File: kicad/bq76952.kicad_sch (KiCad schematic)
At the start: 61 parts, among them Q1 FCX495TA, U4 BQ76952

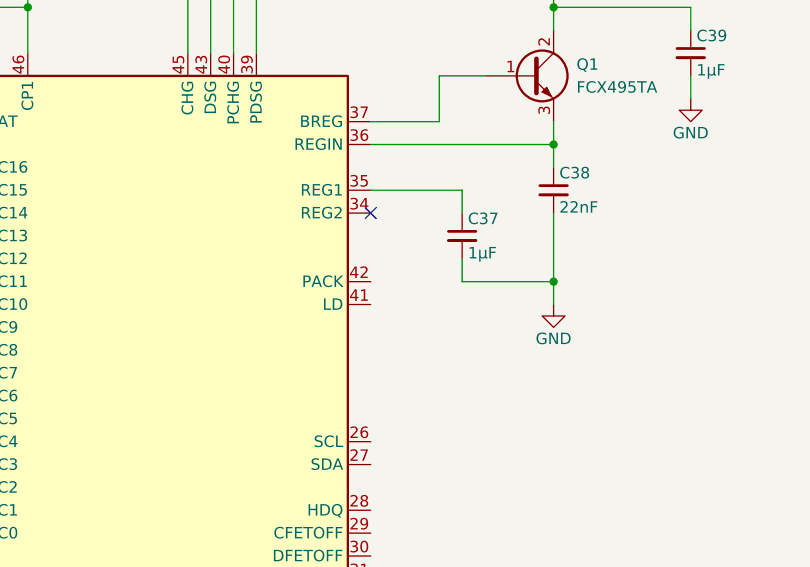
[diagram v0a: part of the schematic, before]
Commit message: Update KiCad files based on spec updates
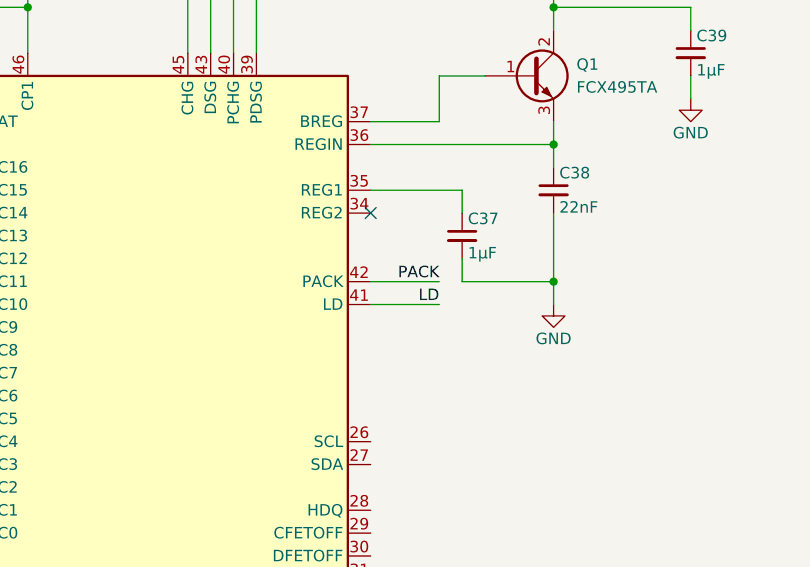
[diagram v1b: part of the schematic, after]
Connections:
- net LD: now reaches U4.41 (LD)
- net PACK: now reaches U4.42 (PACK)
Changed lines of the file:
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@@
     (stroke (width 0) (type solid) (color 0 0 0 0))
+  )
+  (wire (pts (xy 149.86 68.58) (xy 157.48 68.58))
+    (stroke (width 0) (type default) (color 0 0 0 0))
   )
   (wire (pts (xy 256.54 66.04) (xy 256.54 68.58))
@@
   (wire (pts (xy 38.1 43.18) (xy 40.64 43.18))
     (stroke (width 0) (type solid) (color 0 0 0 0))
+  )
+  (wire (pts (xy 149.86 71.12) (xy 157.48 71.12))
+    (stroke (width 0) (type default) (color 0 0 0 0))
   )
   (wire (pts (xy 38.1 165.1) (xy 40.64 165.1))
@@
     (effects (font (size 2.54 2.54)) (justify left bottom))
   )
+  (label "PACK" (at 157.48 68.58 180)
+    (effects (font (size 1.27 1.27)) (justify right bottom))
+  )
   (label "VC13" (at 96.52 63.5 0)
     (effects (font (size 1.27 1.27)) (justify left bottom))
@@
     (effects (font (size 1.27 1.27)) (justify left bottom))
   )
+  (label "LD" (at 157.48 71.12 180)
+    (effects (font (size 1.27 1.27)) (justify right bottom))
+  )
   (hierarchical_label "CELL5+" (shape input) (at 38.1 134.62 180)

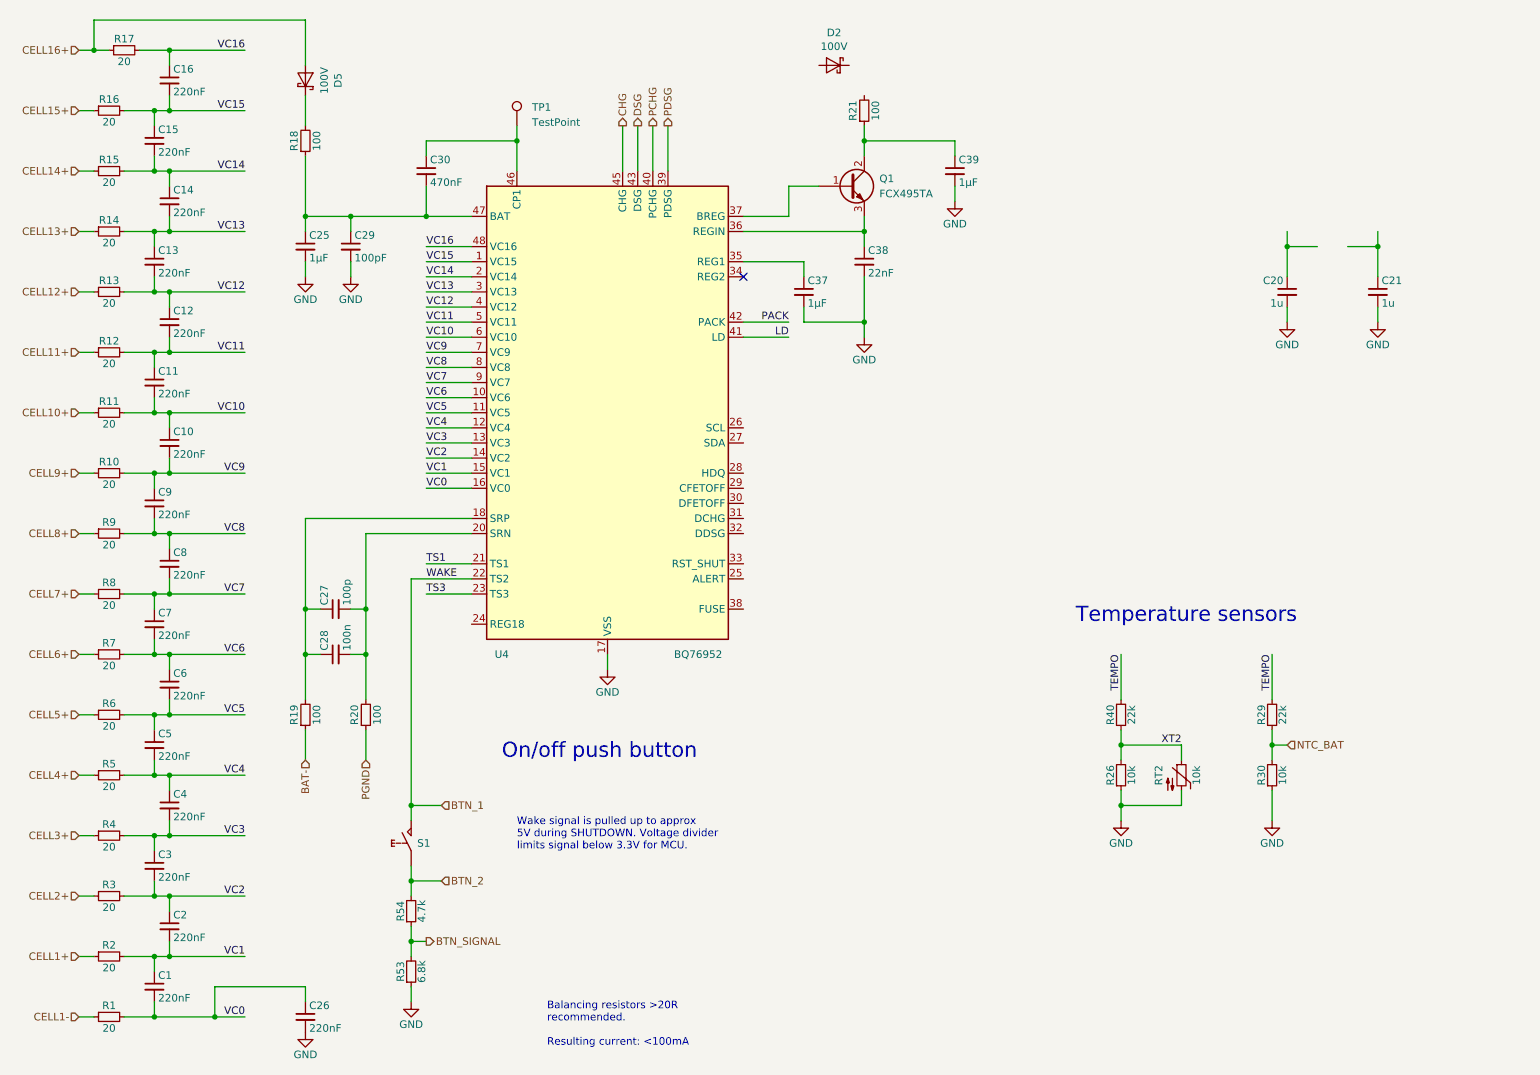
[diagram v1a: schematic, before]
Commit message: WIP: Schematic almost finished
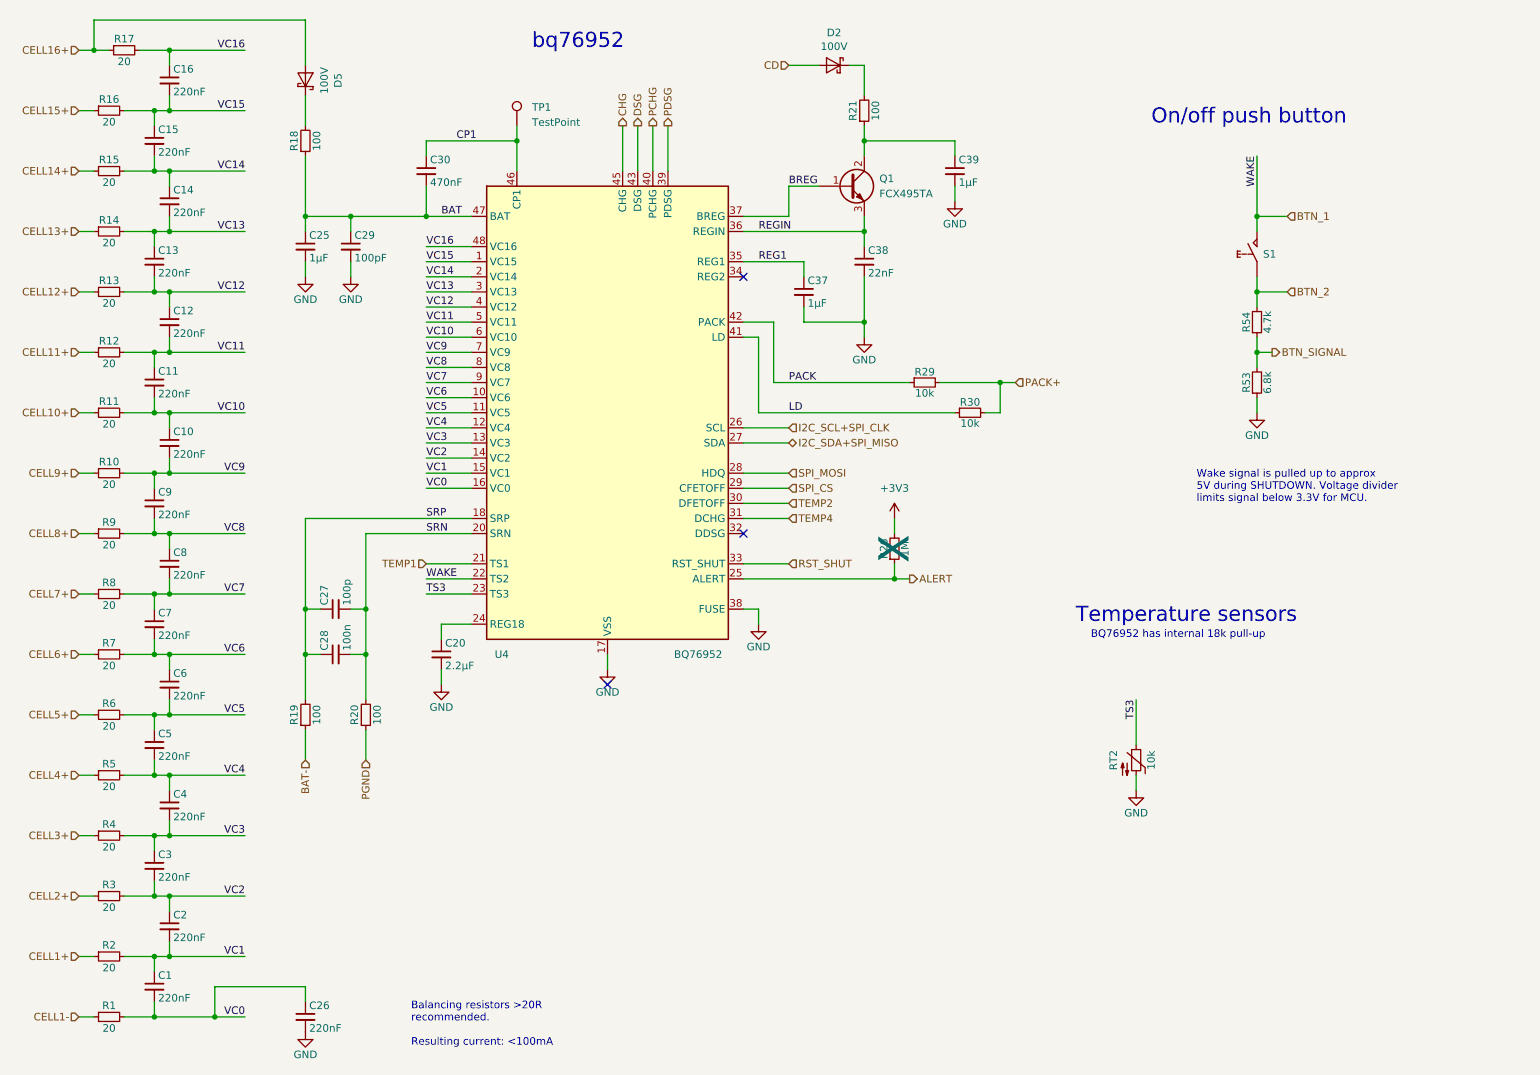
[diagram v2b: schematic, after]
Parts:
- removed C21: 1u, LibreSolar:C_0603_1608, symbol LibreSolar:C
- removed R40: 22k, LibreSolar:R_0603_1608, symbol LibreSolar:R
- C20: value 1u -> 2.2µF; Manufacturer Murata -> any; PartNumber GRT188R61H105KE13D -> (none); Remarks 50V, X5R -> X7R, 6.3V
- R26: value 10k -> 1M; DNM (none) -> X; Manufacturer Yageo -> any; PartNumber RC0603FR-0710KL -> (none)
- R29: value 22k -> 10k; PartNumber RC0603FR-0722KL -> RC0603FR-0710KL
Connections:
- net TEMPO is gone; now on net PACK+: R29.2
- net GND: now also U4.38 (FUSE); no longer R26.1, R30.1
- net LD: now also R30.1
- net PACK: now also R29.1
- net TS3: now also RT2.1
- net SRP: now reaches C27.1, C28.1, R19.2, U4.18 (SRP)
- net SRN: now reaches C27.2, C28.2, R20.2, U4.20 (SRN)
- net at C20.1: now also U4.24 (REG18)
- net BREG: now reaches Q1.1 (B), U4.37 (BREG)
- net REGIN: now reaches C38.1, Q1.3 (E), U4.36 (REGIN)
- net CP1: now reaches C30.1, TP1.1, U4.46 (CP1)
- net BAT: now reaches C25.1, C29.1, C30.2, R18.1, U4.47 (BAT)
- net at R21.2: now also D2.1 (K)
- net CD: now reaches D2.2 (A)
- net ALERT: now reaches U4.25 (ALERT)
- net ALERT: now also R26.1
- net I2C_SCL+SPI_CLK: now reaches U4.26 (SCL)
- net I2C_SDA+SPI_MISO: now reaches U4.27 (SDA)
- net SPI_MOSI: now reaches U4.28 (HDQ)
- net SPI_CS: now reaches U4.29 (CFETOFF)
- net TEMP2: now reaches U4.30 (DFETOFF)
- net TEMP4: now reaches U4.31 (DCHG)
- net RST_SHUT: now reaches U4.33 (RST_SHUT)
- net REG1: now reaches C37.1, U4.35 (REG1)
- net NTC_BAT renamed PACK+
- net PACK+: no longer R29.1
- net TS1 renamed TEMP1
- net XT2 renamed +3V3
- net +3V3: no longer RT2.1
- no-connect marks 1 -> 3
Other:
- note added: "BQ76952 has internal 18k pull-up"
- note added: "bq76952"
- title: BMS 8S50 IC -> BMS 16S Control Board
- moved on the sheet: R53, R54, RT2, S1

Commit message: v0.1 design ready for review
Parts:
- added C44: 1µF, LibreSolar:C_0603_1608, symbol LibreSolar:C
- added C45: 100pF, LibreSolar:C_0603_1608, symbol LibreSolar:C
- added D6: D_Schottky, Diode_SMD:D_SOD-123F, symbol Device:D_Schottky
- added TP15: WAKE, TestPoint:TestPoint_Pad_D1.5mm, symbol Connector:TestPoint
- C27: value 100p -> 100pF; Manufacturer (none) -> any; Remarks (none) -> 100V, C0G/NP0
- C28: value 100n -> 100nF; Manufacturer (none) -> any
- C30: value 470nF -> 680nF
- R18, R21: footprint LibreSolar:R_0603_1608 -> LibreSolar:R_1206_3216
- R29, R30: Manufacturer Yageo -> any; PartNumber RC0603FR-0710KL -> (none)
- R53: Manufacturer Yageo -> any; PartNumber RC0603FR-071ML -> (none)
- R54: Manufacturer Yageo -> any; PartNumber RC0603FR-071KL -> (none)
- TP1: footprint TestPoint:TestPoint_Pad_D2.0mm -> TestPoint:TestPoint_Pad_D1.5mm
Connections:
- net BTN_1: now also TP15.1
- net GND: now also C44.2, C45.2
- net TS3: now also C45.1
- net BREG_IN: now reaches C39.1, Q1.2 (C), R21.1
- net REG2: now reaches U4.34 (REG2)
- net REG2: now also C44.1, D6.2 (A)
- net PCHG: no longer names the net of U4.40 (PCHG)
- net PGND renamed PACK-
- new net +5V: D6.1 (K)
- no-connect marks 3 -> 2
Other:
- note added: "Maximum C_iss of IPT015N10N5 = 16nF CP capacity estimation: 4 x 16nF x 10 = 640nF"
- note added: "Preliminary power supply for MCU after wake-up (see TI reference design) (alternative: REG1 enabling the SMPS)"
- note added: "WAKE"
- moved on the sheet: C27, C38, C39, D2, Q1, R21

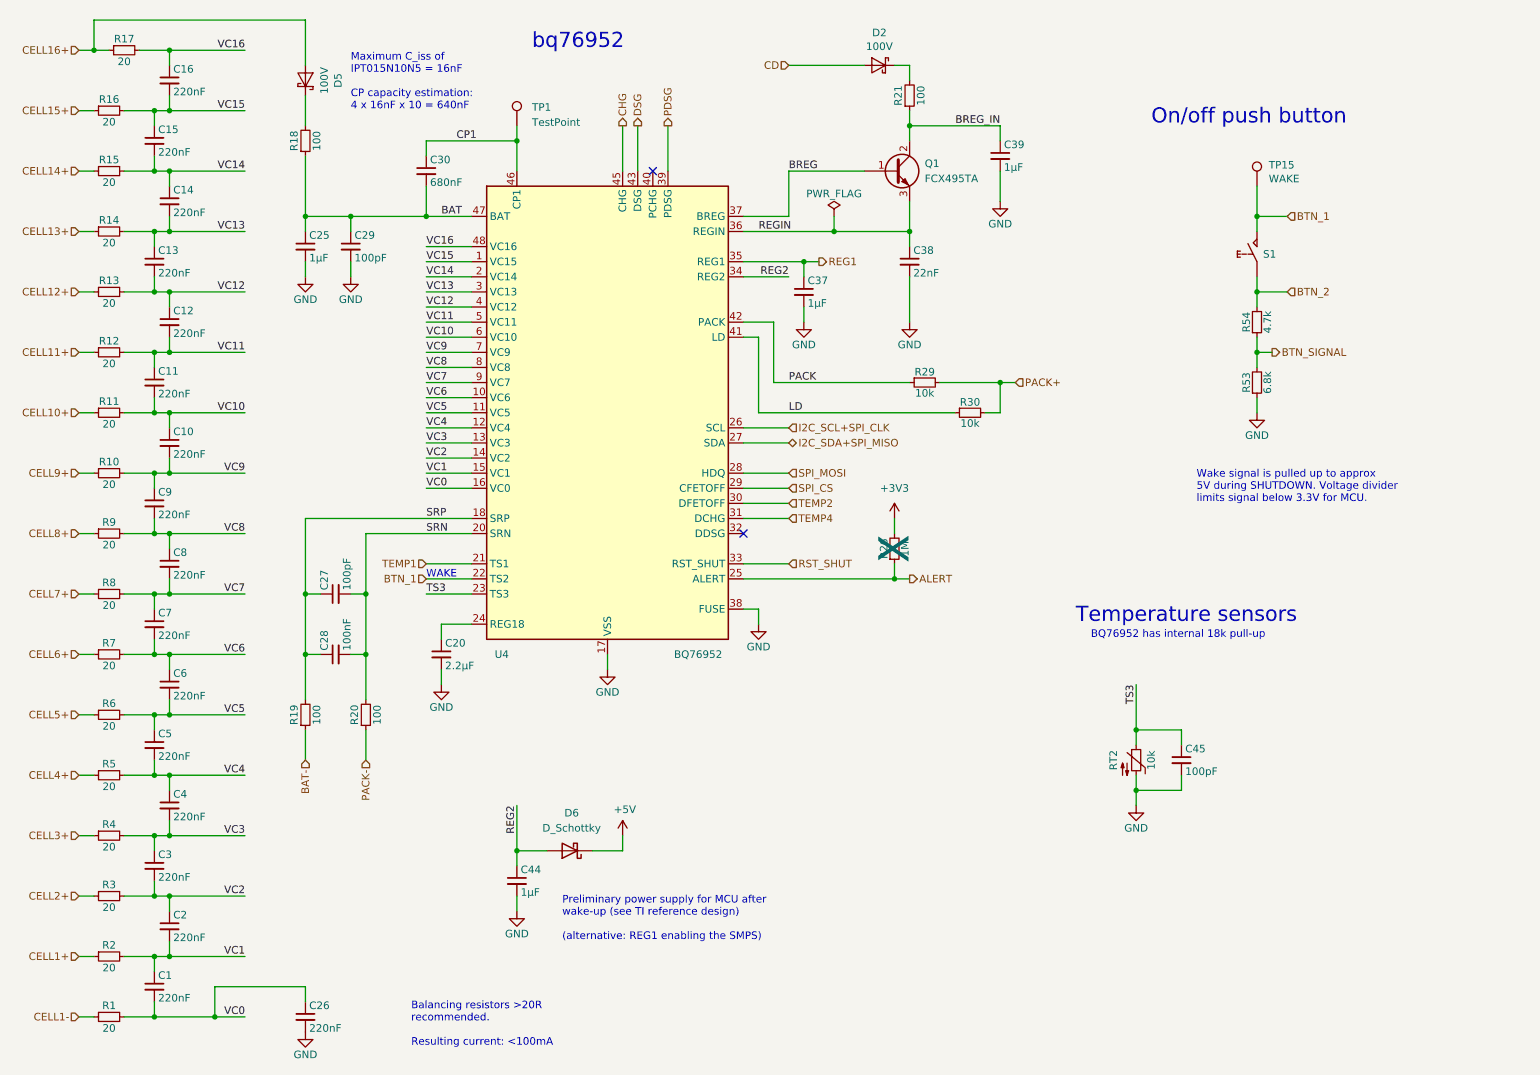
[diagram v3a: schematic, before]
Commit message: Updates based on review comments (v0.2)
This is the design revision that was ordered for the first prototype build.

The pinout of the cell connector and the board-to-board connector changed
compared to v0.1, hence it got a minor revision update.

The control board is now a 4-layer board to improve the grounding of the
PCB. Various other suggested improvements from the design review are also
included in this update.

Fixes #11, #12, #13, #17, #18, #19
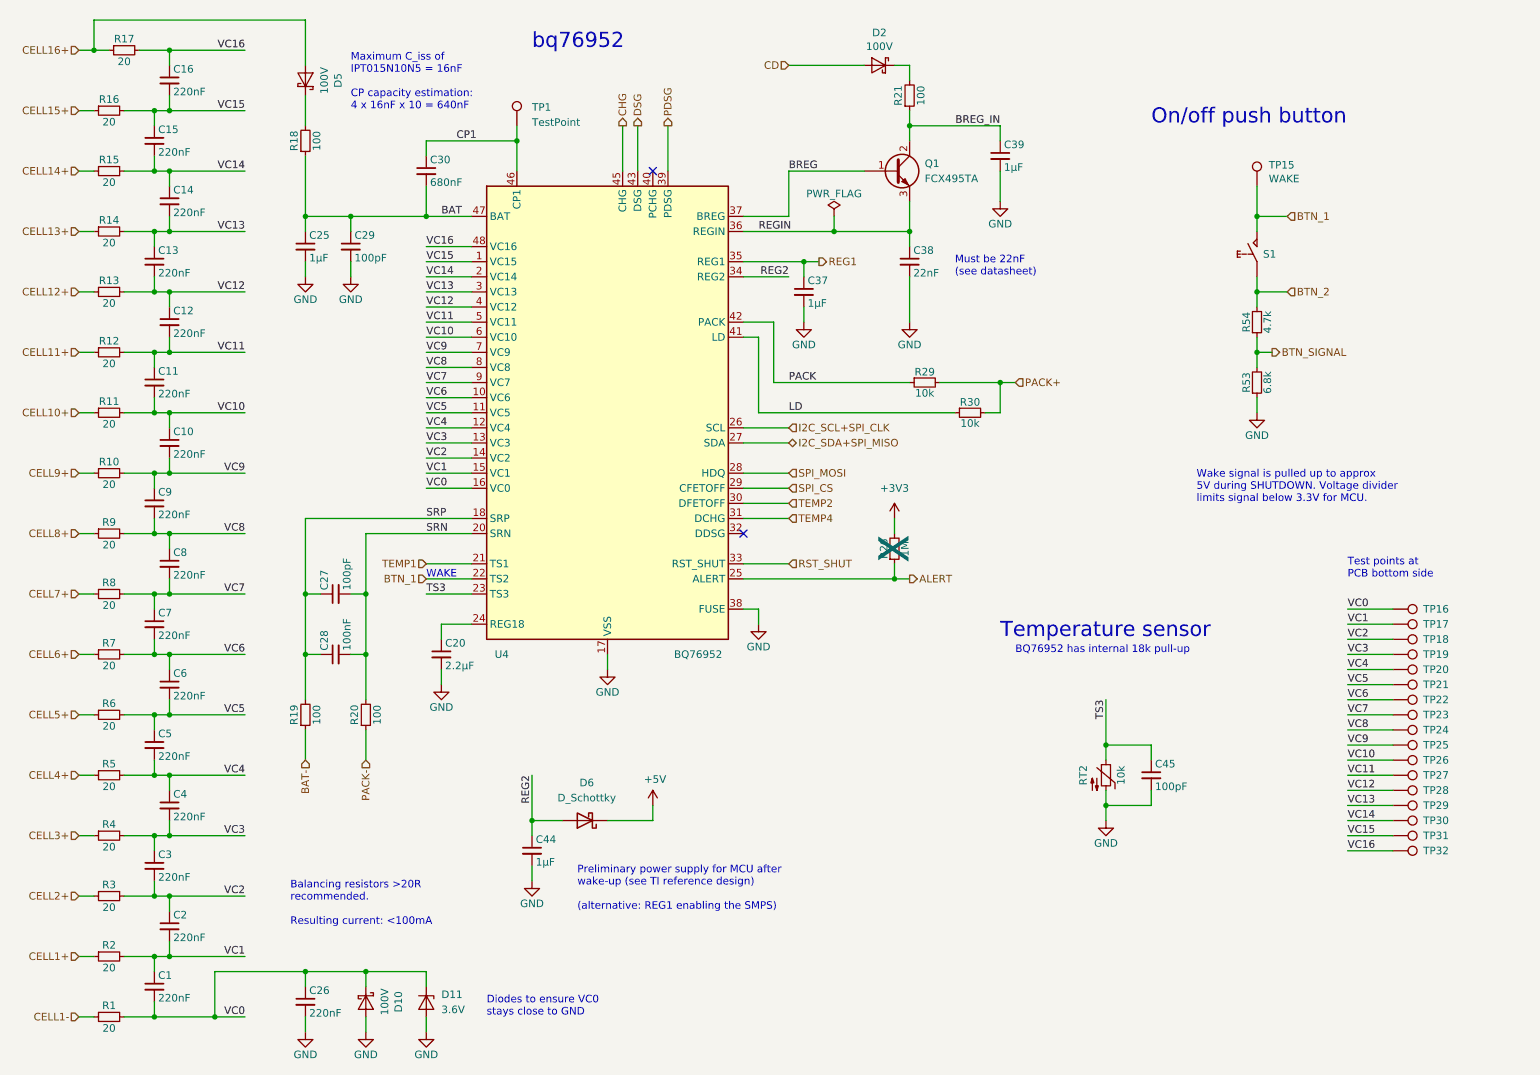
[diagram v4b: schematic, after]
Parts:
- added D10: 100V, Diode_SMD:D_SOD-123, symbol LibreSolar:D_Schottky
- added D11: 3.6V, Diode_SMD:D_SOD-123, symbol LibreSolar:D_Zener
- added TP16, TP17, TP18, TP19, TP20, TP21, TP22, TP23, TP24, TP25, TP26, TP27, TP28, TP29, TP30, TP31, TP32: TestPoint, TestPoint:TestPoint_Pad_D1.5mm, symbol Connector:TestPoint
- C20: Remarks X7R, 6.3V -> X7R, 10V
- U4: Manufacturer (none) -> Texas Instruments; PartNumber (none) -> BQ76952PFBR
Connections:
- net GND: now also D10.2 (A), D11.2 (A)
- net VC0: now also D10.1 (K), D11.1 (K), TP16.1
- net VC1: now also TP17.1
- net VC10: now also TP26.1
- net VC11: now also TP27.1
- net VC12: now also TP28.1
- net VC13: now also TP29.1
- net VC14: now also TP30.1
- net VC15: now also TP31.1
- net VC16: now also TP32.1
- net VC2: now also TP18.1
- net VC3: now also TP19.1
- net VC4: now also TP20.1
- net VC5: now also TP21.1
- net VC6: now also TP22.1
- net VC7: now also TP23.1
- net VC8: now also TP24.1
- net VC9: now also TP25.1
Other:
- note added: "Diodes to ensure VC0 stays close to GND"
- note added: "Must be 22nF (see datasheet)"
- note added: "Temperature sensor"
- note added: "Test points at PCB bottom side"
- note removed: "Temperature sensors"
- moved on the sheet: C26, C44, C45, D6, RT2
